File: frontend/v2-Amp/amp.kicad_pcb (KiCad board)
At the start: 4 copper layers, 80 x 100 mm, 162 parts, among them K1 HK4100, K10 HK4100, K11 HK4100, K12 HK4100, K13 HK4100, K14 HK4100, K15 HK4100, K2 HK4100, K3 HK4100, K4 HK4100, K5 HK4100, K6 HK4100, K7 HK4100, K8 HK4100, K9 HK4100, P1 Antenna, P2 CONN_02X06, P4 TX-IN, P5 RX IN, P6 12-13.8v, Q1 2N3688A, Q2 RD16HHF1, T1 OUT_TRANSF, T2 OUT_TRANSF, U1 LP2951-50D

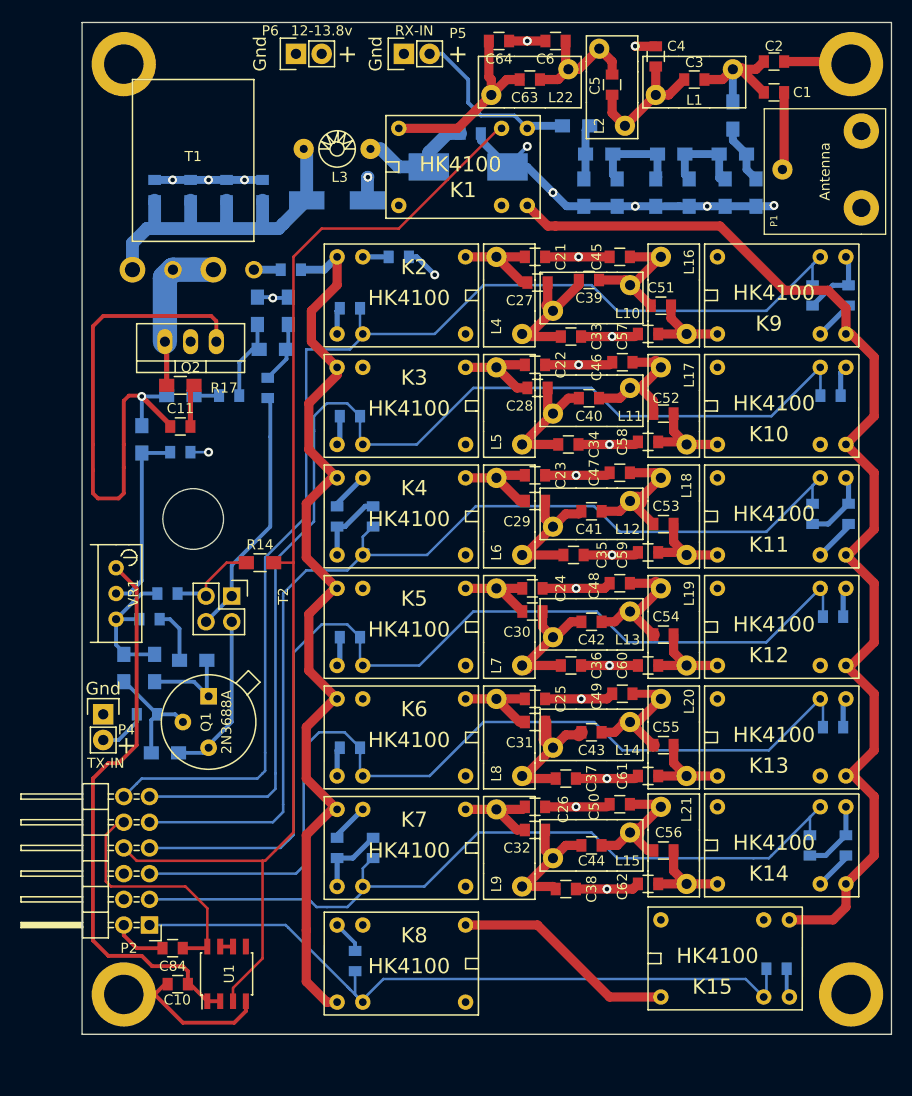
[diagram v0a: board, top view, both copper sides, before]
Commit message: Completion of Norton addition
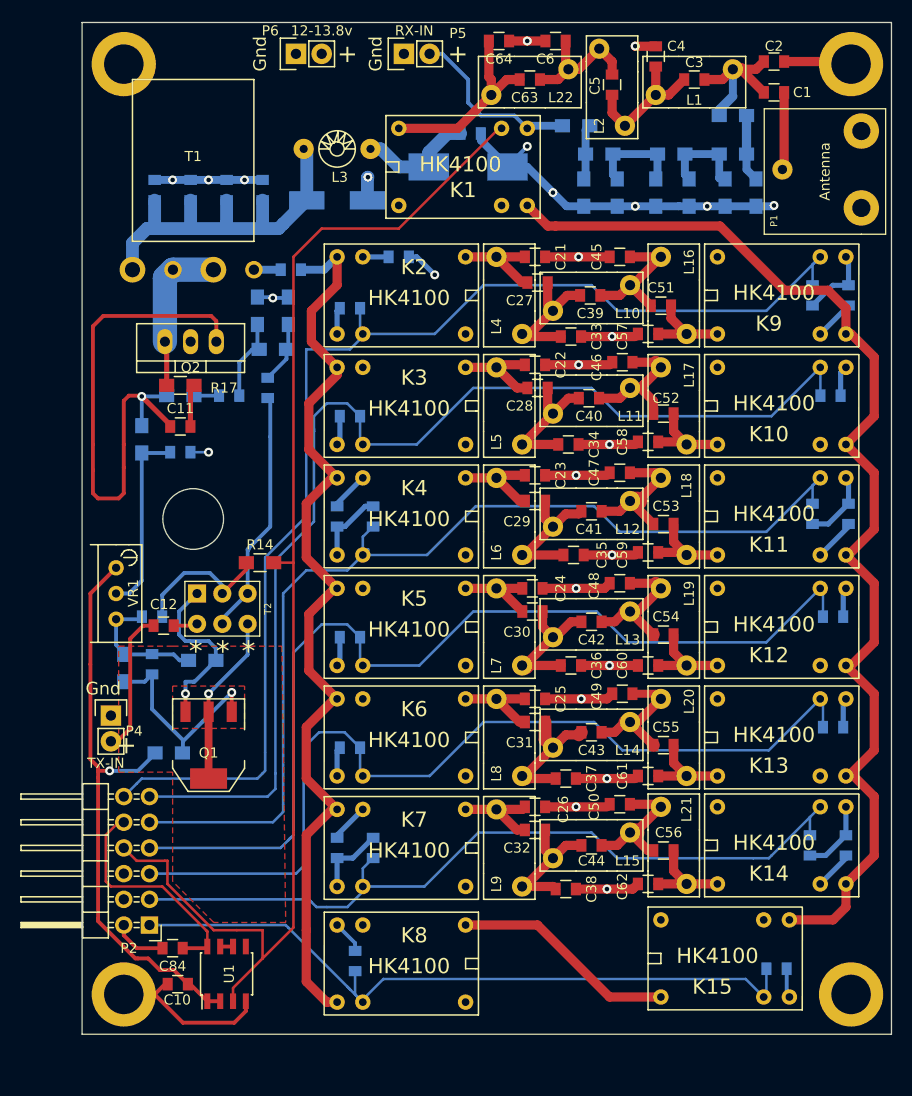
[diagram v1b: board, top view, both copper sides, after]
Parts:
- removed R13: 51, Resistors_SMD:R_0805_HandSoldering
- C10: value 10uF -> 1uF
- C12: moved to F.Cu
- Q1: value 2N3688A -> PZT2222A-T; footprint HERMESLITE:TO39EBC -> TO_SOT_Packages_SMD:SOT-223
- R11: value 470 -> 1k
- R18: value 4.7 -> 47
- R9: value 2k -> 1k
- T2: value OUT_TRANSF -> TRANSFO2; footprint Pin_Headers:Pin_Header_Straight_2x02 -> HERMESLITE:TRANSF
- moved C12 8.92 mm to (123.1, 94.6)
- moved C85 4.45 mm to (121.9, 98.4), turned to 90 degrees
- moved T2 3.44 mm to (126.4, 91.4)
- moved C87 2.75 mm to (121.9, 93.7)
- moved Q1 2.29 mm to (127.5, 106.4), turned to 180 degrees
- moved C39 1.53 mm to (165.2, 62.0)
- moved R18 0.89 mm to (126.9, 98.0)
- moved P4 0.77 mm to (117.9, 103.5)
- moved R9 0.38 mm to (123.6, 107.2), turned to 180 degrees
- turned R1 to 180 degrees
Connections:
- C85 pad 1: GND -> Net-(C85-Pad1)
- C85 pad 2: Net-(C85-Pad2) -> GND
- Q1 pad 1: Net-(Q1-Pad1) -> Net-(C85-Pad1)
- Q1 pad 2: Net-(C12-Pad2) -> Net-(Q1-Pad2)
- R11 pad 2: Net-(C12-Pad2) -> Net-(C85-Pad1)
- R18 pad 1: Net-(C85-Pad2) -> GND
- R18 pad 2: Net-(Q1-Pad1) -> Net-(Q1-Pad3)
- R9 pad 1: Net-(C12-Pad2) -> Net-(C85-Pad1)
- R9 pad 2: Net-(Q1-Pad3) -> Net-(C10-Pad2)
- T2 pad 1: Net-(C86-Pad1) -> Net-(Q1-Pad3)
- T2 pad 2: Net-(Q1-Pad3) -> Net-(C12-Pad2)
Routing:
- net Net-(C85-Pad1): track 0.00 -> 21.4 mm, vias 0 -> 1
- net GND: track 246.1 -> 266.3 mm
- net Net-(Q1-Pad2): track 0.00 -> 16.9 mm, vias 0 -> 1
- net Net-(Q1-Pad1): track 9.56 -> 0.00 mm
- net Net-(C12-Pad2): track 12.0 -> 2.62 mm
- net Net-(C12-Pad1): track 4.81 -> 14.2 mm
- net /PTT: track 118.2 -> 125.0 mm
- net +12v: track 368.3 -> 375.1 mm
- net Net-(C85-Pad2): track 5.48 -> 0.00 mm
- net Net-(C10-Pad2): track 55.9 -> 58.1 mm, vias 0 -> 1
- net Net-(C1-Pad2): track 13.8 -> 15.8 mm
- net Net-(C27-Pad1): track 15.0 -> 13.6 mm
- net Net-(R1-Pad1): track 5.87 -> 6.66 mm
- net Net-(Q1-Pad3): track 16.7 -> 17.1 mm, vias 0 -> 1
- added copper zone on F.Cu, net Net-(Q1-Pad2)
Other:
- board text added: "*"

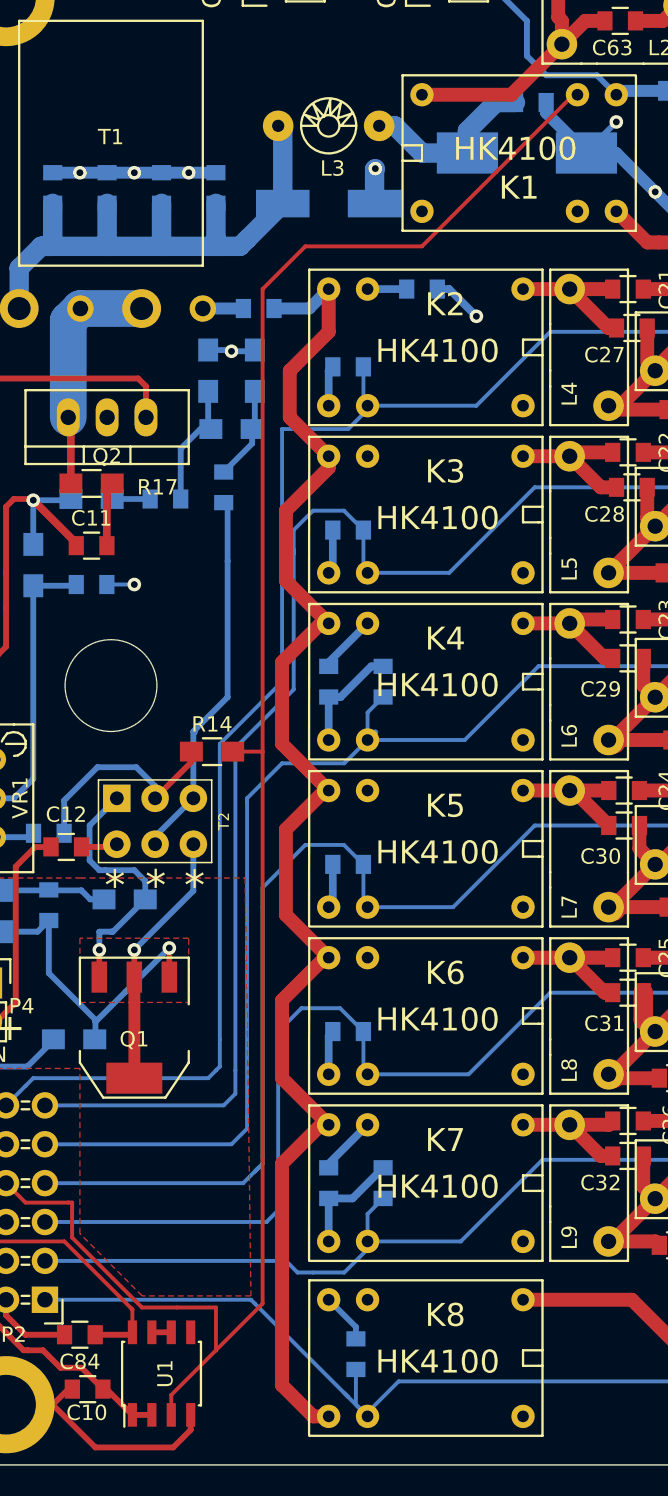
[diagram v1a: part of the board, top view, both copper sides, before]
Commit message: additional R added in preamp
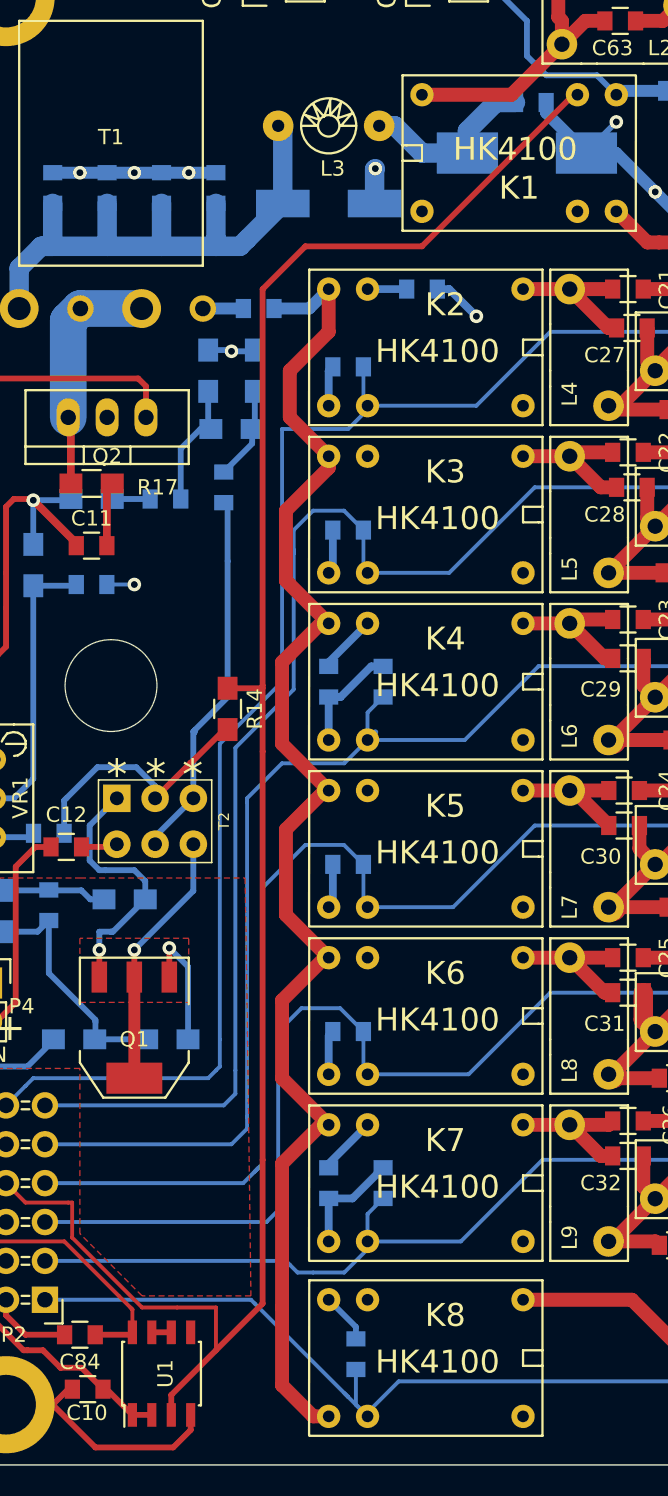
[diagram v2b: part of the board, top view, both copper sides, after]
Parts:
- added R13: 4.7, Resistors_SMD:R_0805_HandSoldering, B.Cu at (129.7, 107.2)
- Q1: value PZT2222A-T -> PZT2222A
- T2: value TRANSFO2 -> BN-43-2402
- moved R14 2.97 mm to (133.6, 85.6), turned to 270 degrees
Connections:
- Q1 pad 1: Net-(C85-Pad1) -> Net-(Q1-Pad1)
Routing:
- net Net-(Q1-Pad1): track 0.00 -> 8.38 mm, vias 0 -> 1
- net Net-(C85-Pad1): track 21.4 -> 16.0 mm, vias 1 -> 0
- net +12v: track 375.1 -> 377.7 mm

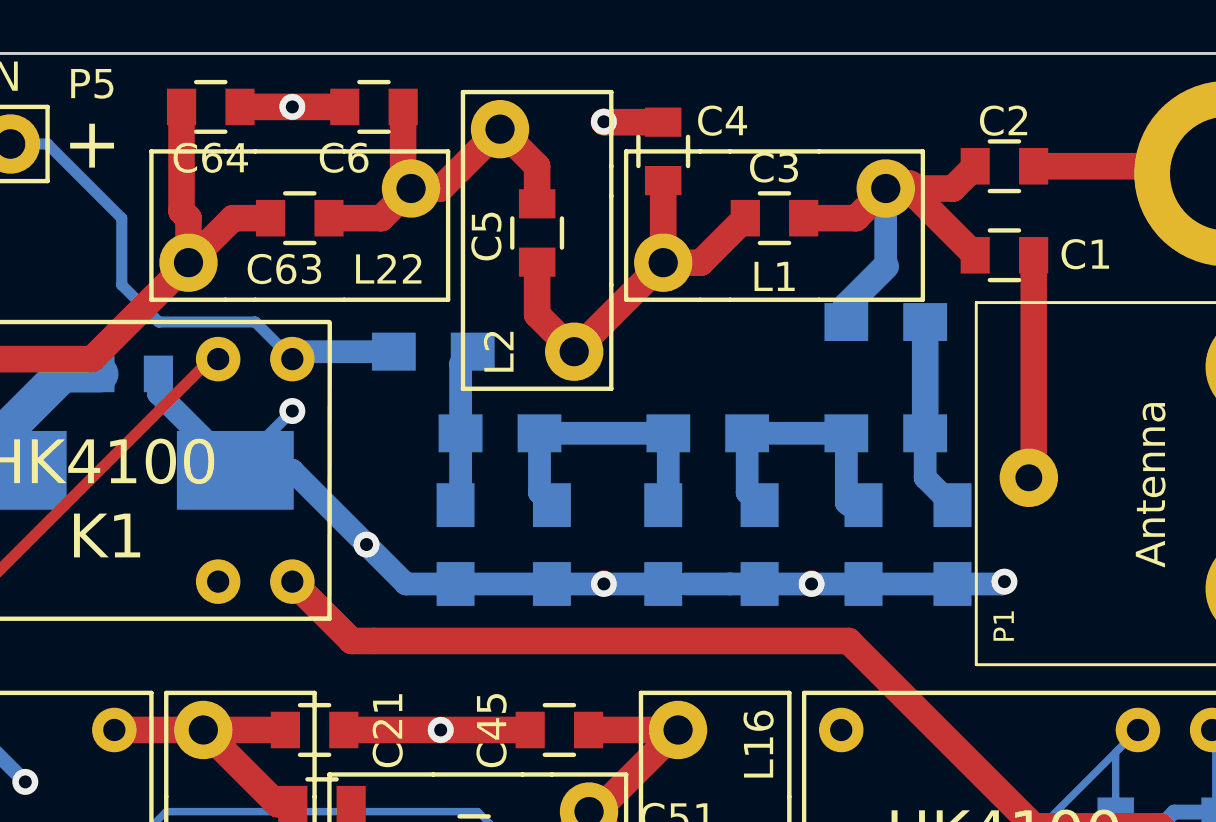
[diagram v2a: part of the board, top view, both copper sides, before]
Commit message: Updates to pure signal tap
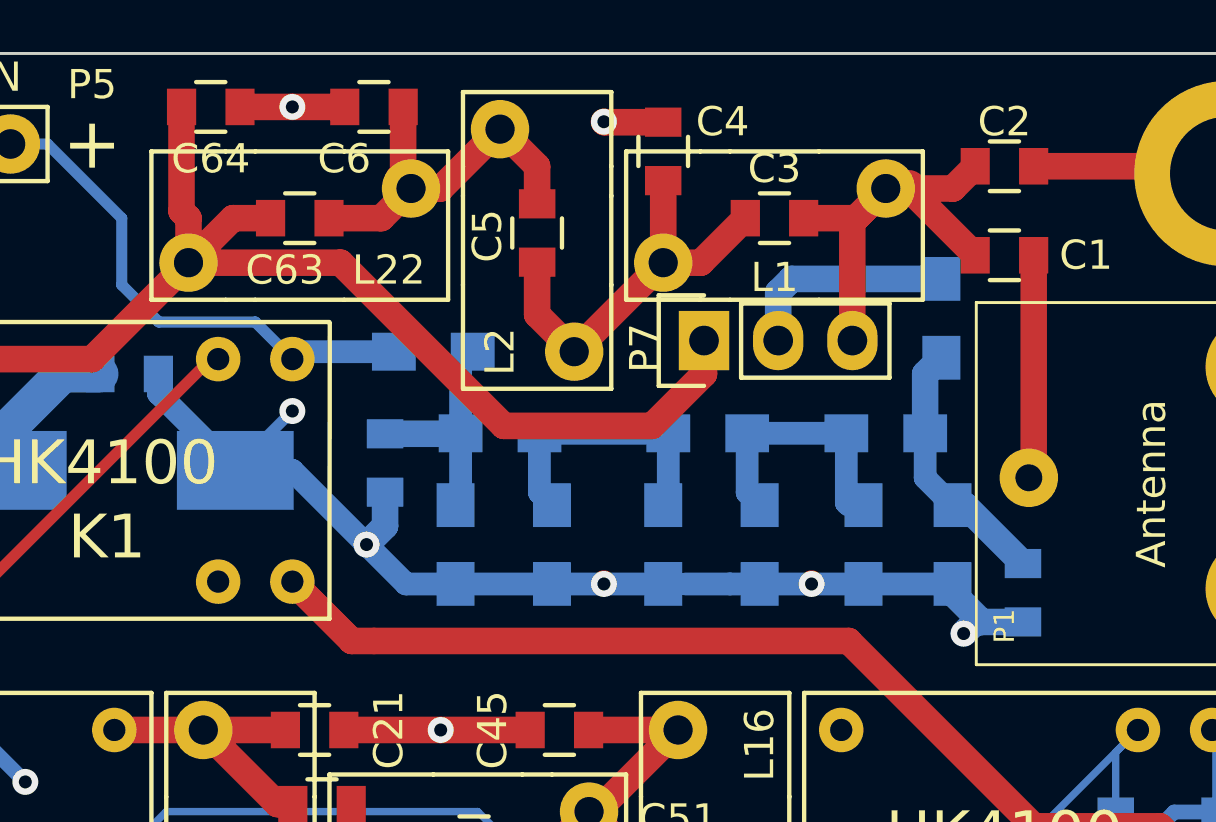
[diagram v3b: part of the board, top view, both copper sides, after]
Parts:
- added C88: DNI, HERMESLITE:C_0805, B.Cu at (184.0, 53.5)
- added C89: DNI, HERMESLITE:C_0805, B.Cu at (162.2, 49.0)
- added P7: CONN_01X03, Pin_Headers:Pin_Header_Straight_1x03, F.Cu at (173.1, 44.8)
- moved R1 1.91 mm to (181.2, 44.1), turned to 90 degrees
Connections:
- R1 pad 2: Net-(C1-Pad2) -> Net-(P7-Pad2)
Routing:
- net Net-(C63-Pad1): track 19.4 -> 41.2 mm
- net Net-(P7-Pad2): track 0.00 -> 7.43 mm
- net GND: track 266.3 -> 270.4 mm
- net Net-(C89-Pad1): track 5.50 -> 8.09 mm
- net Net-(C88-Pad1): track 6.66 -> 8.91 mm
- net Net-(C1-Pad2): track 15.8 -> 16.3 mm

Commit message: 1.0 fab version
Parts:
- removed R25, R4: 120, Resistors_SMD:R_0805_HandSoldering
- added P3: Tap Enable, Pin_Headers:Pin_Header_Straight_1x02, F.Cu at (161.9, 46.4)
- P7: value CONN_01X03 -> Tap Source
- R5, R7: value 160 -> 68
- moved C89 4.59 mm to (165.6, 52.1)
- moved R27 3.43 mm to (168.0, 51.8)
- moved R2 3.18 mm to (178.4, 51.9)
- moved C88 2.79 mm to (181.6, 52.1)
- moved R26 2.54 mm to (168.7, 47.9)
- moved R28 2.27 mm to (164.8, 47.2), turned to 90 degrees
- moved R6 0.77 mm to (174.0, 47.9)
- moved R3 0.13 mm to (179.3, 47.9)
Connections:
- R28 pad 1: Net-(K1-Pad1) -> Net-(P3-Pad2)
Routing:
- net GND: track 270.4 -> 254.6 mm, vias 26 -> 24
- net Net-(R26-Pad2): track 10.1 -> 6.01 mm
- net /PTT: track 125.4 -> 128.7 mm, vias 0 -> 1
- net Net-(R3-Pad1): track 8.53 -> 5.36 mm
- net Net-(P3-Pad2): track 0.00 -> 3.05 mm
- net Net-(U1-Pad6): track 1.27 -> 4.31 mm
- net Net-(C63-Pad1): track 41.2 -> 42.7 mm
- net Net-(C89-Pad1): track 8.09 -> 9.29 mm

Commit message: more changd for v2
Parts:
- removed P7: Tap Source, Pin_Headers:Pin_Header_Straight_1x03
- added R19: 10k, Resistors_SMD:R_0805_HandSoldering, F.Cu at (133.6, 130.9)
- added R4: 39k, Resistors_SMD:R_0805_HandSoldering, F.Cu at (125.6, 138.2)
- C23: value 270pF -> 360pF
- C24: value 270pF -> 180pF
- C25, C61: value 180pF -> 100pF
- C29: value DNI -> 100pf
- C30: value DNI -> 43pF
- C36: value 560pF -> 300pF
- C37, C49: value 390pF -> 270pF
- C41: value DNI -> 300pf
- C42: value DNI -> 130pF
- C47: value 680pF -> 270pF
- C48: value 560pF -> 130pF
- C54: value DNI -> 0R Res
- C59: value 270pF -> 240pF
- C60: value 270pF -> DNI
- L12: value 1.698uH -> 676nH
- L13: value 1.257uH -> 455uH
- L14: value 904nH -> 668nH
- L18: value 1.38uH -> 576nH
- L19: value 1.09uH -> DNI
- L20, L8: value 773nH -> 548nH
- L6: value 1.38uH -> 1.156uH
- L7: value 1.09uH -> 642.5uH
- P3: value Tap Enable -> TX Power Tap
- R9: value 1k -> 1.2k
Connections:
- K15 pad 2: +12v -> /Band6
- K15 pad 5: /Band6 -> +12v
- P3 pad 1: Net-(K1-Pad1) -> GND
- R1 pad 2: Net-(P7-Pad2) -> Net-(C1-Pad2)
- U1 pad 2: Net-(C10-Pad2) -> Net-(U1-Pad2)
- U1 pad 7: Net-(U1-Pad6) -> Net-(R19-Pad2)
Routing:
- net /Band6: track 72.3 -> 163.9 mm
- net +12v: track 377.7 -> 286.2 mm
- net Net-(C63-Pad1): track 42.7 -> 19.4 mm
- net Net-(P7-Pad2): track 7.43 -> 0.00 mm
- net Net-(U1-Pad6): track 4.31 -> 0.00 mm
- net GND: track 254.6 -> 258.2 mm
- net Net-(K1-Pad1): track 17.9 -> 14.4 mm
- net Net-(C10-Pad2): track 58.1 -> 56.8 mm
